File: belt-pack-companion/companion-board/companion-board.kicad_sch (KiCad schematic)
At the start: 54 parts, among them J1 Conn_01x18_Socket, J2 Conn_01x18_Socket, J3 AudioJack4_Ground, J4 Micro_SD_Card, J5 AudioJack3, Q1 MMBT3904, Q2 MMBT3904, U1 TLV320AIC3204

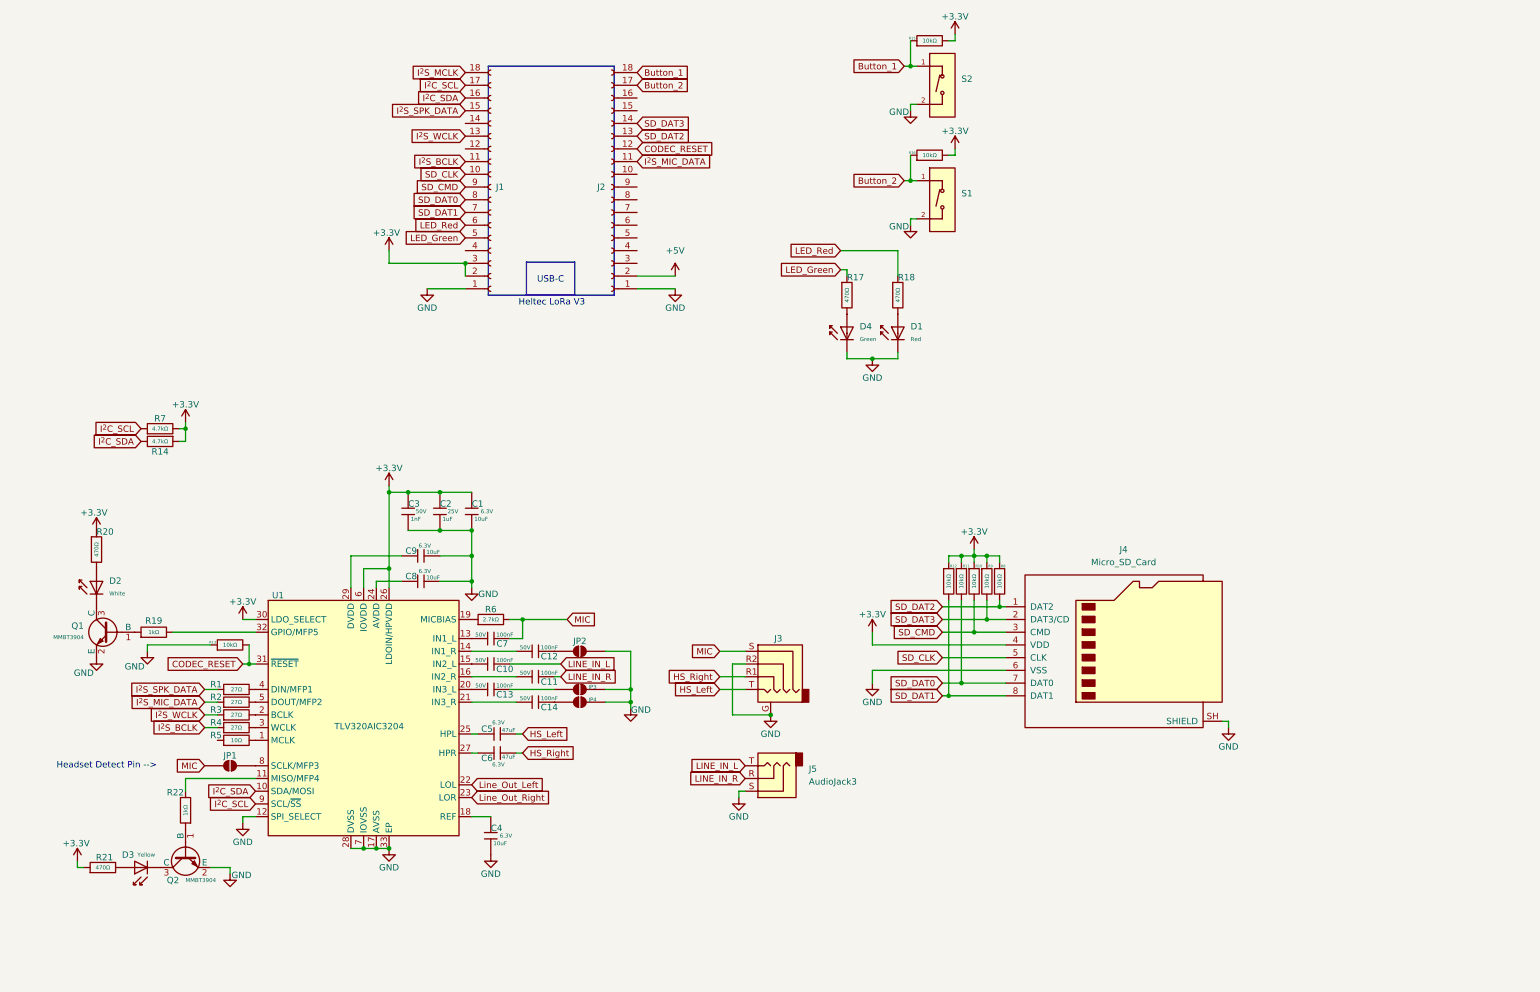
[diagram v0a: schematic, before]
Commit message: Schematic additions
Added 24.576 MHz clock generator.
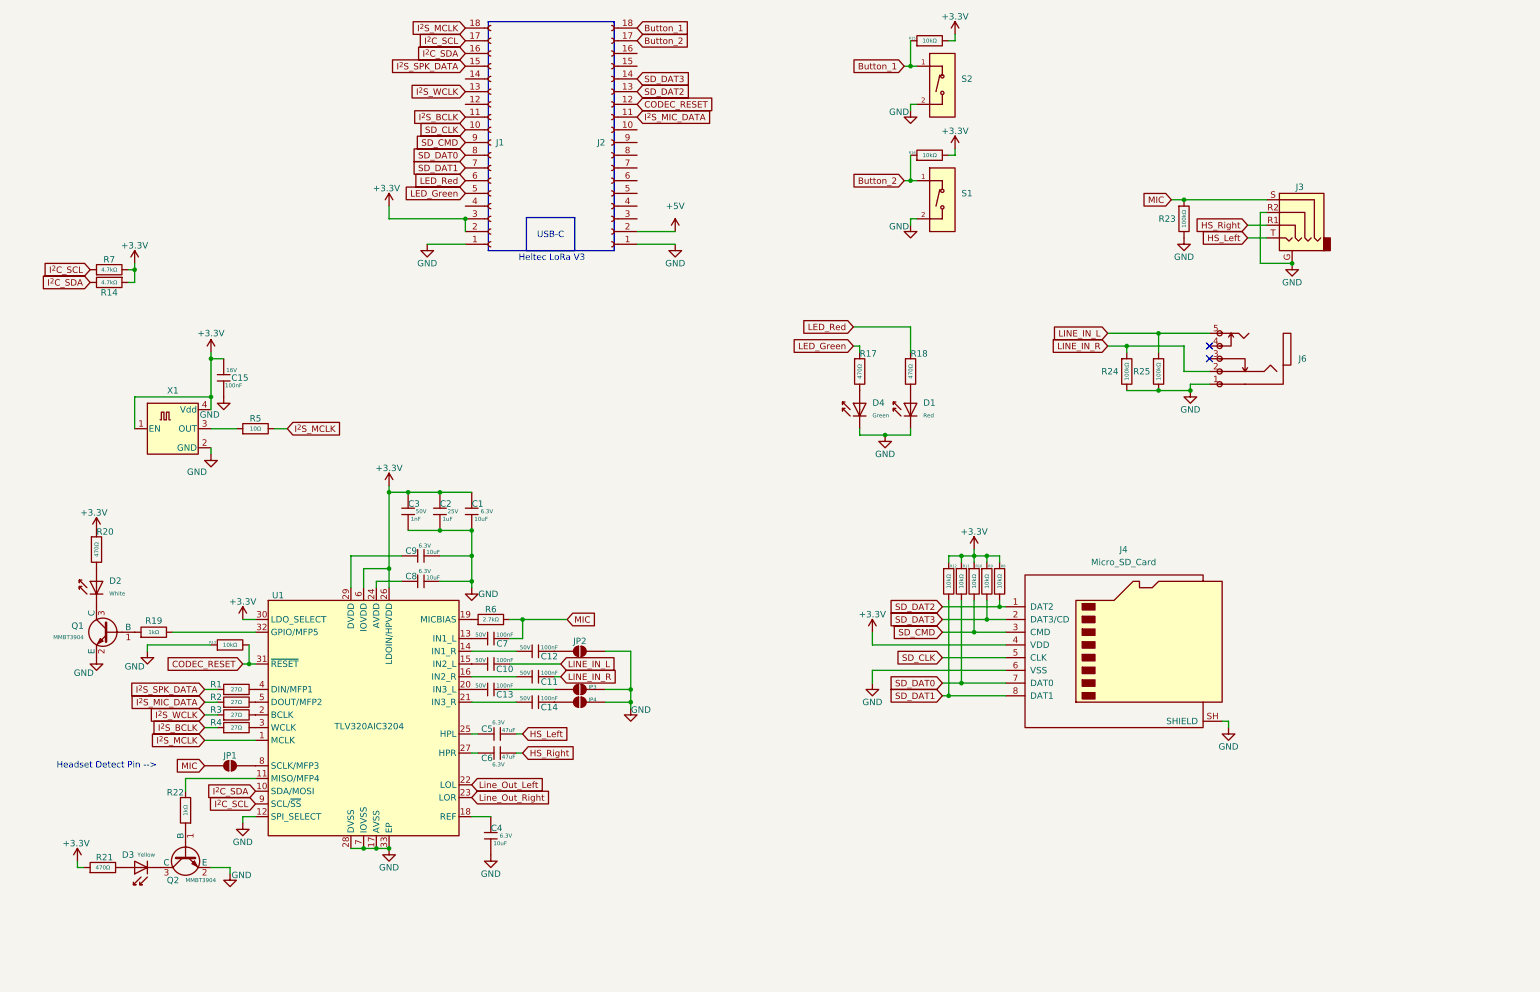
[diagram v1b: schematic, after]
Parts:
- removed J5: AudioJack3, symbol Connector_Audio:AudioJack3
- added C15: 100nF, PCM_JLCPCB:C_0402, symbol PCM_JLCPCB-Capacitors:0402,100nF
- added J6: (no value), EasyEDA_Lib:AUDIO-TH_PJ307C, symbol EasyEDA_Lib:PJ-307C
- added R23, R24, R25: 100kΩ, PCM_JLCPCB:R_0402, symbol PCM_JLCPCB-Resistors:0402,100kΩ
- added X1: YC24.576MUBCE2O, Oscillator:Oscillator_SMD_Abracon_ASE-4Pin_3.2x2.5mm, symbol Oscillator:ASE-xxxMHz
- J1, J2: footprint (none) -> Connector_PinSocket_2.54mm:PinSocket_1x18_P2.54mm_Vertical
- J3: footprint (none) -> EasyEDA_Lib:AUDIO-TH_PJ-3401
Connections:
- net +3.3V: now also C15.1, X1.1 (EN), X1.4 (Vdd)
- net GND: now also C15.2, J6.1, R23.2, R24.2, R25.2, X1.2 (GND)
- net I^{2}S_MCLK: now also R5.2, U1.1 (MCLK)
- net LINE_IN_L: now also J6.5, R25.1
- net LINE_IN_R: now also J6.2, R24.1
- net MIC: now also R23.1
- net at R5.1: now also X1.3 (OUT)
- no-connect marks 0 -> 2
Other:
- moved on the sheet: D1, D4, J1, J2, J3, R14, R17, R18, R7

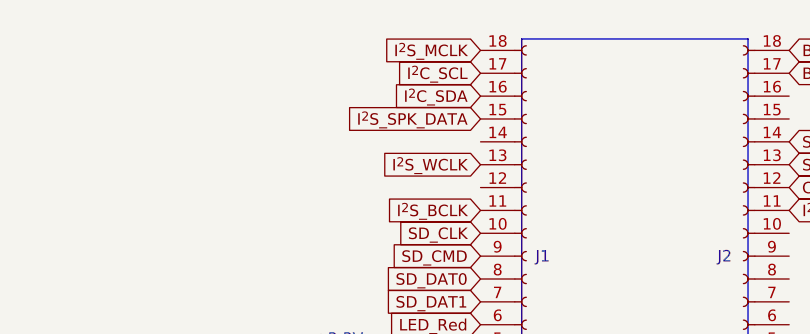
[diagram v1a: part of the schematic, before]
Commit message: Removed MCLK input to ESP32
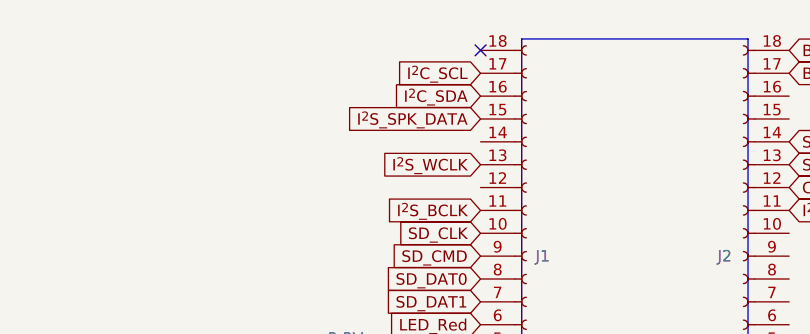
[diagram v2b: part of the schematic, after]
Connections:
- net I^{2}S_MCLK: no longer J1.18 (Pin_18)
- no-connect marks 2 -> 3
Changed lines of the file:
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@@
 	)
 	(no_connect
+		(at 104.14 19.05)
+	)
+	(no_connect
 		(at 252.73 82.55)
 	)
@@
 			)
 		)
-	)
-	(global_label "I^{2}S_MCLK"
-		(shape input)
-		(at 104.14 19.05 180)
-		(fields_autoplaced yes)
-		(effects
-			(font
-				(size 1.27 1.27)
-			)
-			(justify right)
-		)
-		(property "Intersheetrefs" "${INTERSHEET_REFS}"
-			(at 92.3858 19.05 0)
-			(hide yes)
-			(show_name no)
-			(do_not_autoplace no)
-			(effects
-				(font
-					(size 1.27 1.27)
-				)
-				(justify right)
-			)
-		)

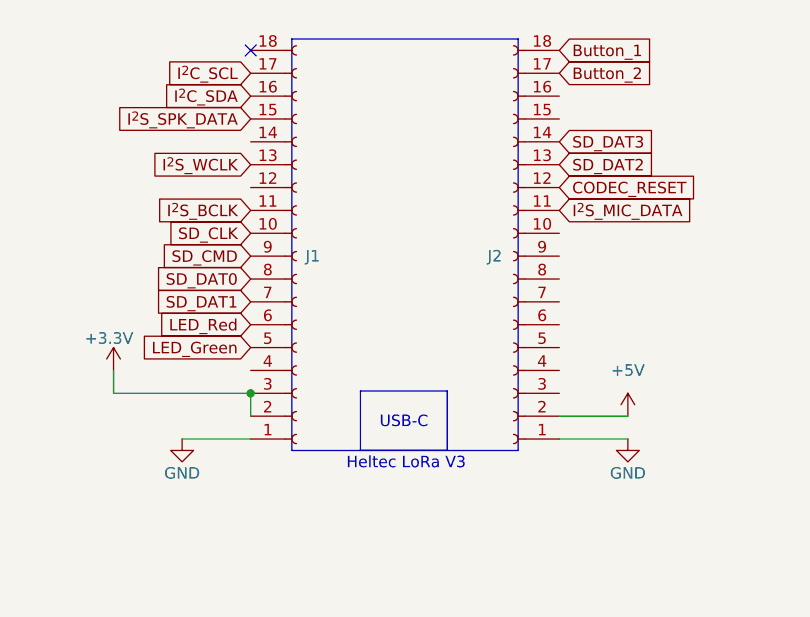
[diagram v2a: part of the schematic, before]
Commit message: Added pin labels and NC to heltec v3
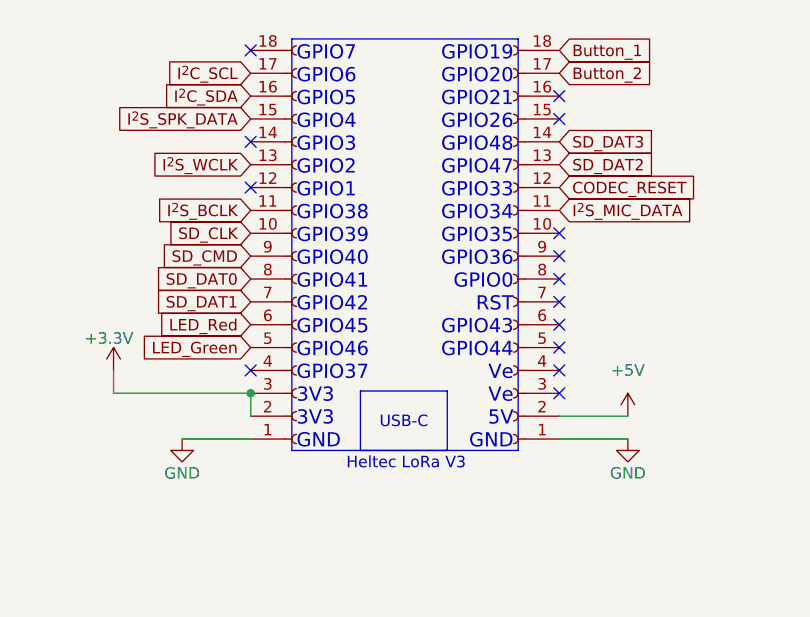
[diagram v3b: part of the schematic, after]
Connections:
- no-connect marks 3 -> 16
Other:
- note added: "GPIO19 GPIO20 GPIO21 GPIO26 GPIO48 GPIO47 GPIO33 GPIO34 GPIO35 GPIO36 GPIO0 RST GPIO43 GPIO44 Ve Ve 5V GND"
- note added: "GPIO7 GPIO6 GPIO5 GPIO4 GPIO3 GPIO2 GPIO1 GPIO38 GPIO39 GPIO40 GPIO41 GPIO42 GPIO45 GPIO46 GPIO37 3V3 3V3 GND"
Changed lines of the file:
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@@
 	)
 	(rectangle
-		(start 108.712 63.5)
-		(end 133.858 17.78)
+		(start 108.712 17.78)
+		(end 133.858 63.5)
 		(stroke
 			(width 0)
@@
 		)
 	)
+	(text "GPIO19\nGPIO20\nGPIO21\nGPIO26\nGPIO48\nGPIO47\nGPIO33\nGPIO34\nGPIO35\nGPIO36\nGPIO0\nRST\nGPIO43\nGPIO44\nVe\nVe\n5V\nGND"
+		(exclude_from_sim no)
+		(at 133.35 18.542 0)
+		(effects
+			(font
+				(size 1.5748 1.5748)
+			)
+			(justify right top)
+		)
+	)
+	(text "GPIO7\nGPIO6\nGPIO5\nGPIO4\nGPIO3\nGPIO2\nGPIO1\nGPIO38\nGPIO39\nGPIO40\nGPIO41\nGPIO42\nGPIO45\nGPIO46\nGPIO37\n3V3\n3V3\nGND"
+		(exclude_from_sim no)
+		(at 109.22 18.542 0)
+		(effects
+			(font
+				(size 1.5748 1.5748)
+			)
+			(justify left top)
+		)
+	)
 	(text "Headset Detect Pin -->"
 		(exclude_from_sim no)
@@
 	)
 	(no_connect
+		(at 138.43 54.61)
+	)
+	(no_connect
+		(at 138.43 44.45)
+	)
+	(no_connect
+		(at 104.14 54.61)
+	)
+	(no_connect
+		(at 104.14 29.21)
+	)
+	(no_connect
+		(at 138.43 57.15)
+	)
+	(no_connect
+		(at 138.43 39.37)
+	)
+	(no_connect
+		(at 138.43 41.91)
+	)
+	(no_connect
+		(at 104.14 34.29)
+	)
+	(no_connect
+		(at 138.43 24.13)
+	)
+	(no_connect
 		(at 252.73 85.09)
 	)
 	(no_connect
+		(at 138.43 46.99)
+	)
+	(no_connect
 		(at 104.14 19.05)
 	)
@@
 		(at 252.73 82.55)
 	)
+	(no_connect
+		(at 138.43 26.67)
+	)
+	(no_connect
+		(at 138.43 49.53)
+	)
+	(no_connect
+		(at 138.43 52.07)
+	)
 	(wire
 		(pts
@@
 		(property "Reference" "J2"
 			(at 132.08 41.91 0)
+			(hide yes)
 			(show_name no)
 			(do_not_autoplace no)
@@
 		(property "Reference" "J1"
 			(at 110.236 41.91 0)
+			(hide yes)
 			(show_name no)
 			(do_not_autoplace no)

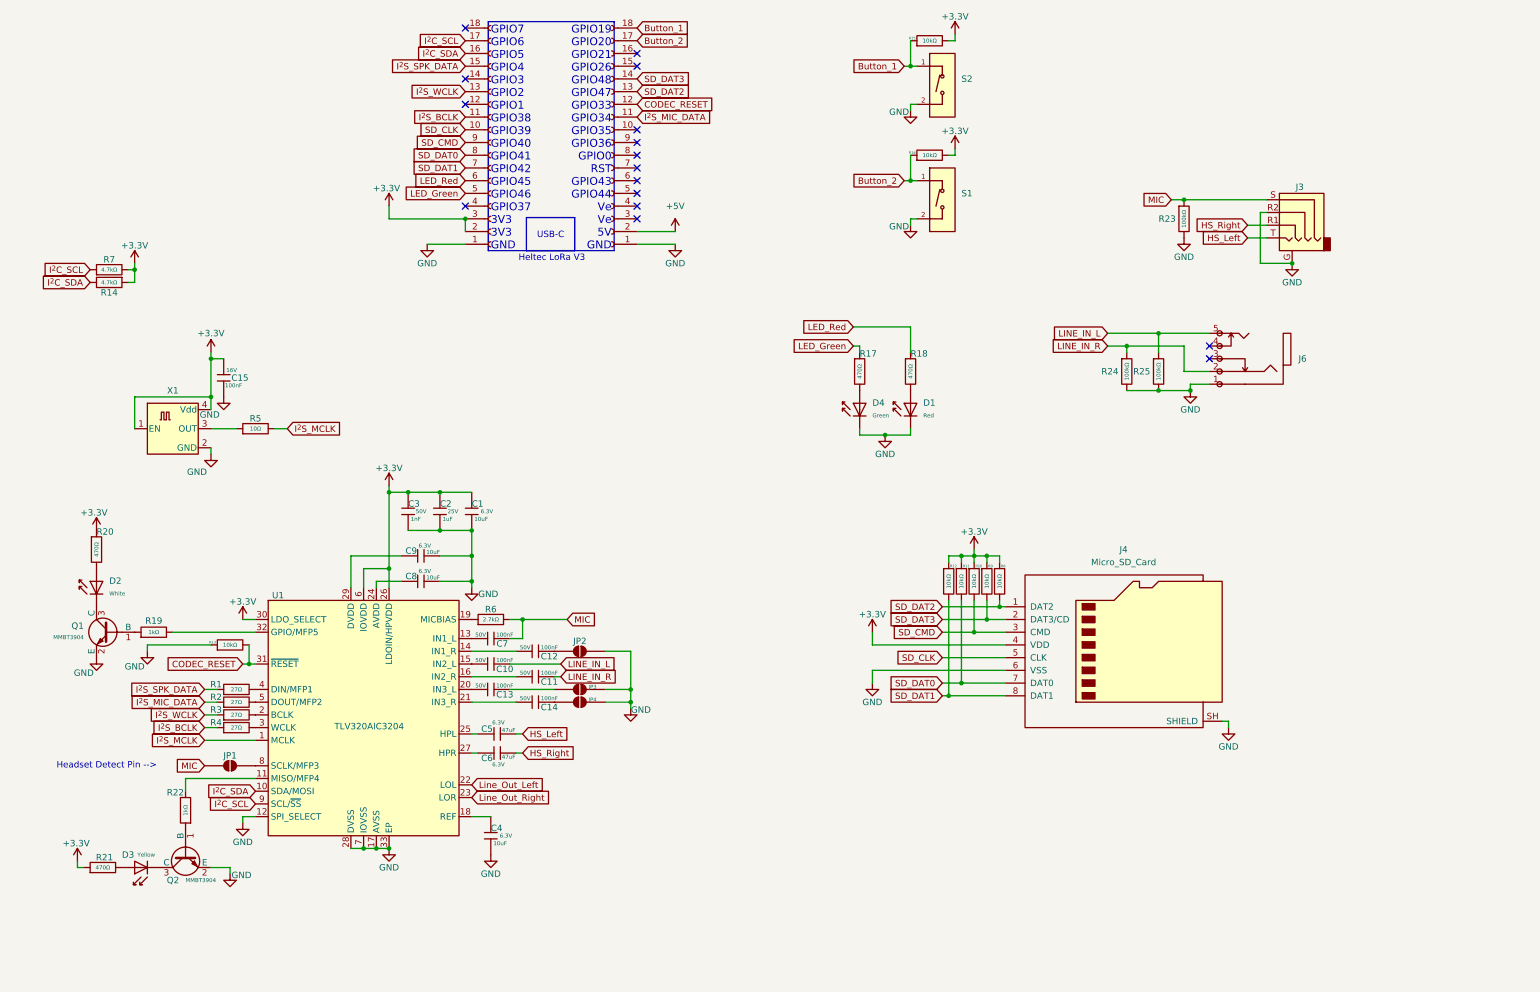
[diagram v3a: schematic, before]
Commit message: JLC'd the audio jack and the sd card slot
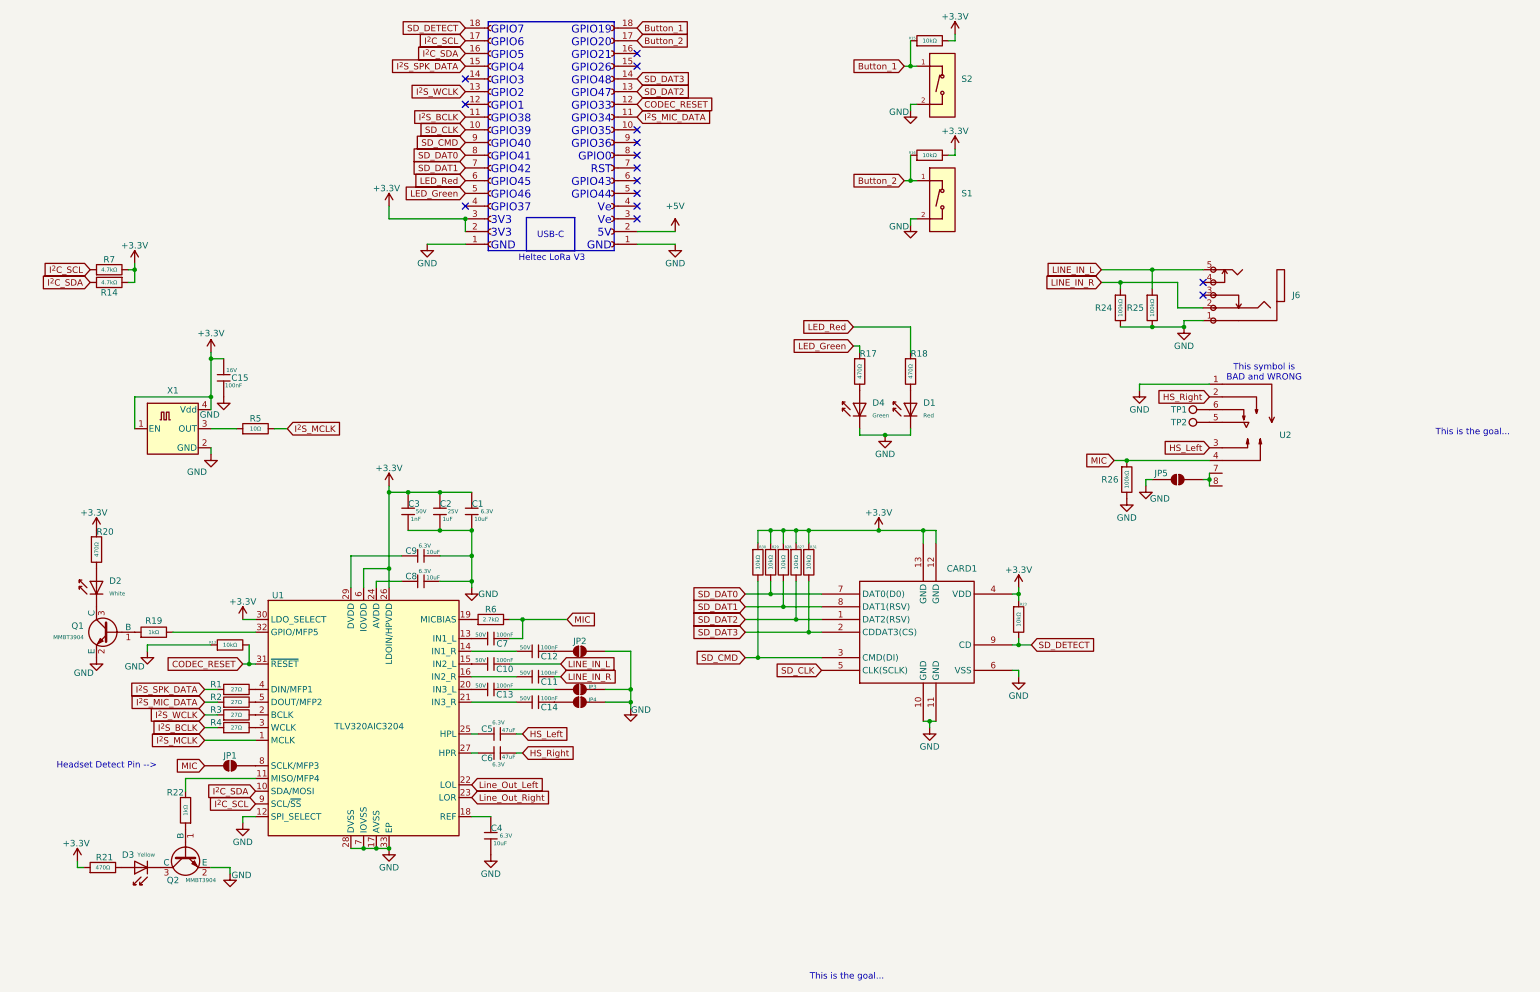
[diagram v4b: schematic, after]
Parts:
- removed J3: AudioJack4_Ground, EasyEDA_Lib:AUDIO-TH_PJ-3401, symbol Connector_Audio:AudioJack4_Ground
- removed J4: Micro_SD_Card, symbol Connector:Micro_SD_Card
- removed R10, R11, R12, R8, R9: 10kΩ, PCM_JLCPCB:R_0402, symbol PCM_JLCPCB-Resistors:0402,10kΩ
- removed R23: 100kΩ, PCM_JLCPCB:R_0402, symbol PCM_JLCPCB-Resistors:0402,100kΩ
- added CARD1: (no value), EasyEDA_Lib:TF-SMD_TF-01A, symbol EasyEDA_Lib:TF-01A
- added JP5: SolderJumper_2_Open, symbol Jumper:SolderJumper_2_Open
- added R23, R27, R28, R29, R30, R31: 10kΩ, PCM_JLCPCB:R_0402, symbol PCM_JLCPCB-Resistors:0402,10kΩ
- added R26: 100kΩ, PCM_JLCPCB:R_0402, symbol PCM_JLCPCB-Resistors:0402,100kΩ
- added TP1, TP2: TestPoint, symbol Connector:TestPoint
- added U2: (no value), EasyEDA_Lib:AUDIO-TH_PJ-3401, symbol EasyEDA_Lib:PJ-3401
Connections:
- net +3.3V: now also CARD1.12 (GND), CARD1.13 (GND), CARD1.4 (VDD), R23.1, R27.1, R28.1, R29.1, R30.1, R31.1
- net GND: now also CARD1.10 (GND), CARD1.11 (GND), CARD1.6 (VSS), JP5.1 (A), R26.2, U2.1 (GND/MIC)
- net HS_Left: now also U2.3 (L)
- net HS_Right: now also U2.2 (R)
- net MIC: now also R26.1, U2.4 (GND/MIC)
- net SD_CLK: now also CARD1.5 (CLK(SCLK))
- net SD_CMD: now also CARD1.3 (CMD(DI)), R30.2
- net SD_DAT0: now also CARD1.7 (DAT0(D0)), R29.2
- net SD_DAT1: now also CARD1.8 (DAT1(RSV)), R28.2
- net SD_DAT2: now also CARD1.1 (DAT2(RSV)), R27.2
- net SD_DAT3: now also CARD1.2 (CDDAT3(CS)), R31.2
- net SD_DETECT: now reaches J1.18 (Pin_18)
- net SD_DETECT: now also CARD1.9 (CD), R23.2
- new net: TP1.1, U2.6
- new net: TP2.1, U2.5
- new net: JP5.2 (B), U2.7 (SHELL), U2.8 (SHELL)
- no-connect marks 16 -> 15
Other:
- note added: "This is the goal..."
- note added: "This symbol is BAD and WRONG"
- moved on the sheet: J6, R24, R25

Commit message: Finished adding footprints
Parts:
- JP5: footprint (none) -> Jumper:SolderJumper-2_P1.3mm_Open_RoundedPad1.0x1.5mm
- TP2: footprint (none) -> TestPoint:TestPoint_Plated_Hole_D2.0mm
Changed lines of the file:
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@@
 			)
 		)
-		(property "Footprint" ""
+		(property "Footprint" "Jumper:SolderJumper-2_P1.3mm_Open_RoundedPad1.0x1.5mm"
 			(at 246.38 109.22 0)
 			(hide yes)
@@
 			)
 		)
-		(property "Footprint" ""
+		(property "Footprint" "TestPoint:TestPoint_Plated_Hole_D2.0mm"
 			(at 252.73 92.71 0)
 			(hide yes)

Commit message: Created and Finished PCB
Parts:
- removed J6: (no value), EasyEDA_Lib:AUDIO-TH_PJ307C, symbol EasyEDA_Lib:PJ-307C
- removed R24, R25: 100kΩ, PCM_JLCPCB:R_0402, symbol PCM_JLCPCB-Resistors:0402,100kΩ
- added J3: (no value), EasyEDA_Lib:AUDIO-TH_PJ313D, symbol EasyEDA_Lib:PJ313D
- added J4: Conn_01x03_Pin, Connector_PinHeader_2.54mm:PinHeader_1x03_P2.54mm_Vertical, symbol Connector:Conn_01x03_Pin
- added R32, R33: 100kΩ, PCM_JLCPCB:R_0402, symbol PCM_JLCPCB-Resistors:0402,100kΩ
- JP1, JP2, JP3, JP4: footprint (none) -> Jumper:SolderJumper-2_P1.3mm_Open_RoundedPad1.0x1.5mm
- TP1: footprint (none) -> TestPoint:TestPoint_THTPad_D2.0mm_Drill1.0mm
- TP2: footprint TestPoint:TestPoint_Plated_Hole_D2.0mm -> TestPoint:TestPoint_THTPad_D2.0mm_Drill1.0mm
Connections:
- net +3.3V: no longer CARD1.12 (GND), CARD1.13 (GND)
- net GND: now also CARD1.12 (GND), CARD1.13 (GND), J3.2, J4.1 (Pin_1), R32.2, R33.2
- net LINE_IN_L: now also J3.4, R32.1
- net LINE_IN_R: now also J3.3, R33.1
- net Line_Out_Left: now also J4.3 (Pin_3)
- net Line_Out_Right: now also J4.2 (Pin_2)
- no-connect marks 15 -> 13
